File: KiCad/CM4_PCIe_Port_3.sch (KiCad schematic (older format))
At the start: 1 part, among them J15 PCIe_x16

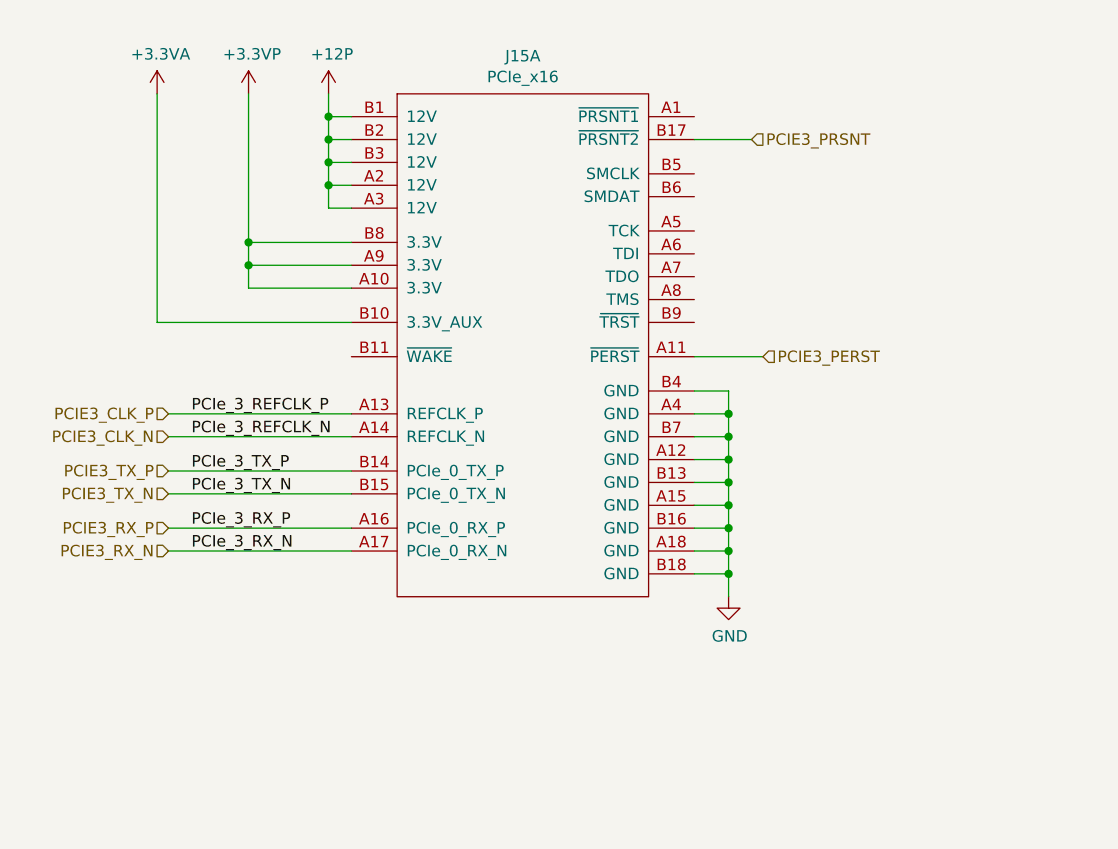
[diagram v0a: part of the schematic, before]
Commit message: Adding PCIe subsystem
- Moves a lot of the PCIe related items from the top level sheet to a new sheet called PCIe Subsystem which then has other hierarchical sheets below it.

- This adds some of the AC coupling caps for the PCIe slots, might need to do some work with the switch yet.

- Adds an SMBUS mux for the SMBUS connections to the PCIe slots. Extra SMBUS lanes sit un-wired and can be used for other things.

- Adds JTAG headers for the PCIe connectors.
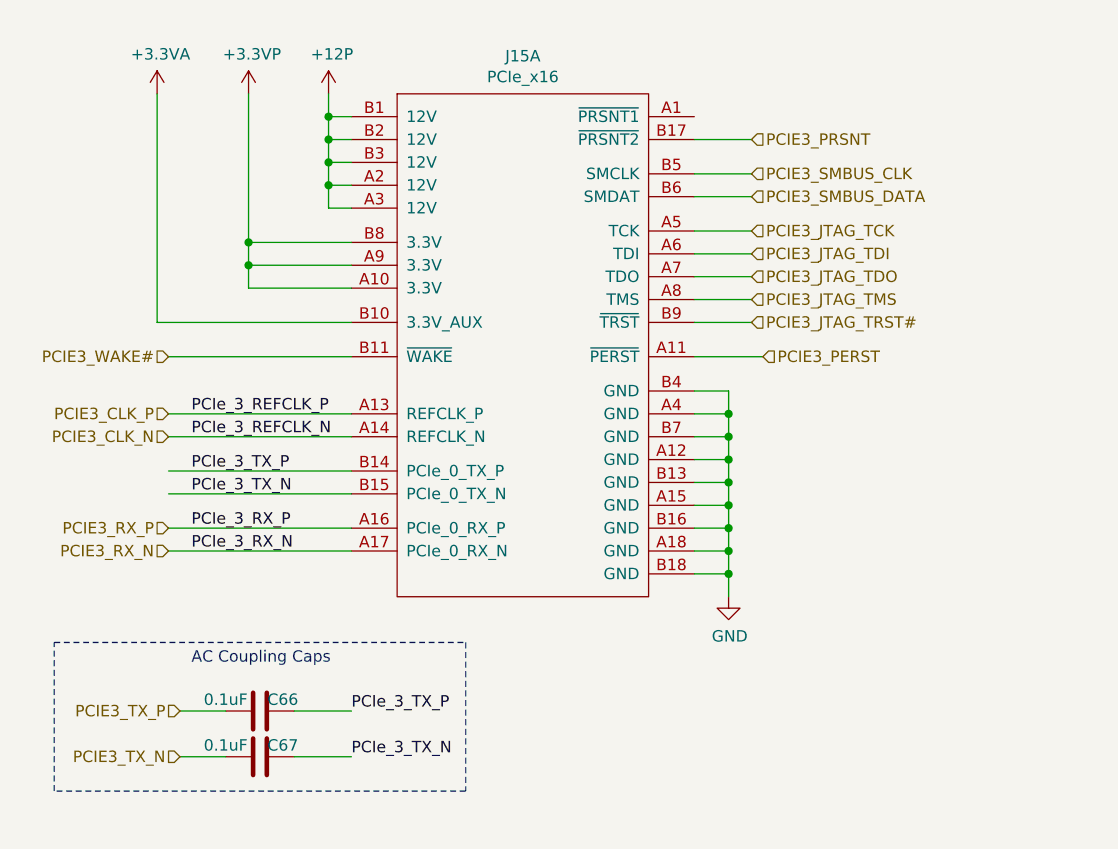
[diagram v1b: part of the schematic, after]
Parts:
- added C66, C67: 0.1uF, symbol CM4_MATX:C
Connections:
- net PCIE3_TX_N: now also C67.2; no longer J15.B15 (PCIe_0_TX_N)
- net PCIE3_TX_P: now also C66.1; no longer J15.B14 (PCIe_0_TX_P)
- net PCIE3_JTAG_TCK: now reaches J15.A5 (TCK)
- net PCIE3_JTAG_TDI: now reaches J15.A6 (TDI)
- net PCIE3_JTAG_TDO: now reaches J15.A7 (TDO)
- net PCIE3_JTAG_TMS: now reaches J15.A8 (TMS)
- net PCIE3_WAKE#: now reaches J15.B11 (~WAKE)
- net PCIE3_SMBUS_CLK: now reaches J15.B5 (SMCLK)
- net PCIE3_SMBUS_DATA: now reaches J15.B6 (SMDAT)
- net PCIE3_JTAG_TRST#: now reaches J15.B9 (~TRST)
- new net PCIe_3_TX_N: C67.1, J15.B15 (PCIe_0_TX_N)
- new net PCIe_3_TX_P: C66.2, J15.B14 (PCIe_0_TX_P)
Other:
- note added: "AC Coupling Caps"
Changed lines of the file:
@@
 $Descr A4 11693 8268
 encoding utf-8
-Sheet 9 12
+Sheet 13 15
 Title ""
 Date "2020-12-28"
@@
 Text HLabel 1300 4450 0    50   Input ~ 0
 PCIE3_RX_P
-Text HLabel 1300 4200 0    50   Input ~ 0
-PCIE3_TX_P
-Text HLabel 1300 4300 0    50   Input ~ 0
-PCIE3_TX_N
 $Comp
 L power:GND #PWR?
@@
 AR Path="/5FCA7683/5FEB60E6" Ref="#PWR?"  Part="1"
 AR Path="/5FD6762E/5FEB60E6" Ref="#PWR0185"  Part="1"
-F 0 "#PWR0185" H 3750 4500 50  0001 C CNN
+AR Path="/5FFBC089/5FFBFF34/5FEB60E6" Ref="#PWR0194"  Part="1"
+F 0 "#PWR0194" H 3750 4500 50  0001 C CNN
 F 1 "GND" H 3755 4577 50  0000 C CNN
 F 2 "" H 3750 4750 50  0001 C CNN
@@
 AR Path="/5FCA7683/5FEB6112" Ref="#PWR?"  Part="1"
 AR Path="/5FD6762E/5FEB6112" Ref="#PWR0186"  Part="1"
-F 0 "#PWR0186" H 2000 2400 50  0001 C CNN
+AR Path="/5FFBC089/5FFBFF34/5FEB6112" Ref="#PWR0195"  Part="1"
+F 0 "#PWR0195" H 2000 2400 50  0001 C CNN
 F 1 "+12P" H 2015 2723 50  0000 C CNN
 F 2 "" H 2000 2550 50  0001 C CNN
@@
 AR Path="/5FCA7683/5FEB6126" Ref="#PWR?"  Part="1"
 AR Path="/5FD6762E/5FEB6126" Ref="#PWR0187"  Part="1"
-F 0 "#PWR0187" H 1800 2500 50  0001 C CNN
+AR Path="/5FFBC089/5FFBFF34/5FEB6126" Ref="#PWR0196"  Part="1"
+F 0 "#PWR0196" H 1800 2500 50  0001 C CNN
 F 1 "+3.3VP" H 1665 2723 50  0000 C CNN
 F 2 "" H 1650 2550 50  0001 C CNN
@@
 AR Path="/5FCA7683/5FEB6134" Ref="#PWR?"  Part="1"
 AR Path="/5FD6762E/5FEB6134" Ref="#PWR0188"  Part="1"
-F 0 "#PWR0188" H 1250 2400 50  0001 C CNN
+AR Path="/5FFBC089/5FFBFF34/5FEB6134" Ref="#PWR0197"  Part="1"
+F 0 "#PWR0197" H 1250 2400 50  0001 C CNN
 F 1 "+3.3VA" H 1265 2723 50  0000 C CNN
 F 2 "" H 1250 2550 50  0001 C CNN
@@
 U 1 1 5FEE686E
 P 2900 4400
+AR Path="/5FD6762E/5FEE686E" Ref="J15"  Part="1"
+AR Path="/5FFBC089/5FFBFF34/5FEE686E" Ref="J15"  Part="1"
 F 0 "J15" H 2850 6415 50  0000 C CNN
 F 1 "PCIe_x16" H 2850 6324 50  0000 C CNN
@@
 U 2 1 5FEE9FE9
 P 8250 3900
+AR Path="/5FD6762E/5FEE9FE9" Ref="J15"  Part="2"
+AR Path="/5FFBC089/5FFBFF34/5FEE9FE9" Ref="J15"  Part="2"
 F 0 "J15" H 8250 5915 50  0000 C CNN
 F 1 "PCIe_x16" H 8250 5824 50  0000 C CNN
@@
 U 3 1 5FEECB70
 P 10100 3400
+AR Path="/5FD6762E/5FEECB70" Ref="J15"  Part="3"
+AR Path="/5FFBC089/5FFBFF34/5FEECB70" Ref="J15"  Part="3"
 F 0 "J15" H 10100 5415 50  0000 C CNN
 F 1 "PCIe_x16" H 10100 5324 50  0000 C CNN
@@
 U 1 1 601661E8
 P 10950 5400
-F 0 "#PWR0193" H 10950 5150 50  0001 C CNN
+AR Path="/5FD6762E/601661E8" Ref="#PWR0193"  Part="1"
+AR Path="/5FFBC089/5FFBFF34/601661E8" Ref="#PWR0198"  Part="1"
+F 0 "#PWR0198" H 10950 5150 50  0001 C CNN
 F 1 "GND" H 10955 5227 50  0000 C CNN
 F 2 "" H 10950 5400 50  0001 C CNN
@@
 U 1 1 60166A1C
 P 9100 5550
-F 0 "#PWR0194" H 9100 5300 50  0001 C CNN
+AR Path="/5FD6762E/60166A1C" Ref="#PWR0194"  Part="1"
+AR Path="/5FFBC089/5FFBFF34/60166A1C" Ref="#PWR0199"  Part="1"
+F 0 "#PWR0199" H 9100 5300 50  0001 C CNN
 F 1 "GND" H 9105 5377 50  0000 C CNN
 F 2 "" H 9100 5550 50  0001 C CNN
@@
 	1    0    0    -1
 $EndComp
+Wire Wire Line
+	1350 5450 1550 5450
+Wire Wire Line
+	1350 5250 1550 5250
+$Comp
+L CM4_MATX:C C?
+U 1 1 5FF316D6
+P 1700 5450
+AR Path="/5FCA7683/5FF316D6" Ref="C?"  Part="1"
+AR Path="/5FFBC089/5FFBFF34/5FF316D6" Ref="C67"  Part="1"
+F 0 "C67" V 1650 5550 50  0000 C CNN
+F 1 "0.1uF" V 1650 5300 50  0000 C CNN
+F 2 "" H 1738 5300 50  0001 C CNN
+F 3 "~" H 1700 5450 50  0001 C CNN
+	1    1700 5450
+	0    1    1    0
+$EndComp
+$Comp
+L CM4_MATX:C C?
+U 1 1 5FF316DC
+P 1700 5250
+AR Path="/5FCA7683/5FF316DC" Ref="C?"  Part="1"
+AR Path="/5FFBC089/5FFBFF34/5FF316DC" Ref="C66"  Part="1"
+F 0 "C66" V 1750 5150 50  0000 C CNN
+F 1 "0.1uF" V 1750 5400 50  0000 C CNN
+F 2 "" H 1738 5100 50  0001 C CNN
+F 3 "~" H 1700 5250 50  0001 C CNN
+	1    1700 5250
+	0    -1   -1   0
+$EndComp
+Wire Wire Line
+	1850 5450 2100 5450
+Wire Wire Line
+	1850 5250 2100 5250
+Text Notes 1400 5050 0    50   ~ 0
+AC Coupling Caps
+Wire Notes Line
+	800  4950 2600 4950
+Wire Notes Line
+	2600 4950 2600 5600
+Wire Notes Line
+	2600 5600 800  5600
+Wire Notes Line
+	800  5600 800  4950
+Text HLabel 1350 5250 0    50   Input ~ 0
+PCIE3_TX_P
+Text HLabel 1350 5450 0    50   Input ~ 0
+PCIE3_TX_N
+Text Label 2100 5450 0    50   ~ 0
+PCIe_3_TX_N
+Text Label 2100 5250 0    50   ~ 0
+PCIe_3_TX_P
+Wire Wire Line
+	3600 2900 3850 2900
+Wire Wire Line
+	3600 3000 3850 3000
+Text HLabel 3850 2900 2    50   Input ~ 0
+PCIE3_SMBUS_CLK
+Text HLabel 3850 3000 2    50   Input ~ 0
+PCIE3_SMBUS_DATA
+Wire Wire Line
+	2100 3700 1300 3700
+Text HLabel 1300 3700 0    50   Input ~ 0
+PCIE3_WAKE#
+Wire Wire Line
+	3600 3150 3850 3150
+Wire Wire Line
+	3600 3250 3850 3250
+Wire Wire Line
+	3600 3350 3850 3350
+Wire Wire Line
+	3600 3450 3850 3450
+Wire Wire Line
+	3600 3550 3850 3550
+Text HLabel 3850 3150 2    50   Input ~ 0
+PCIE3_JTAG_TCK
+Text HLabel 3850 3250 2    50   Input ~ 0
+PCIE3_JTAG_TDI
+Text HLabel 3850 3350 2    50   Input ~ 0
+PCIE3_JTAG_TDO
+Text HLabel 3850 3450 2    50   Input ~ 0
+PCIE3_JTAG_TMS
+Text HLabel 3850 3550 2    50   Input ~ 0
+PCIE3_JTAG_TRST#
 $EndSCHEMATC
